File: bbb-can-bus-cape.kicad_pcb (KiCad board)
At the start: 2 copper layers, 54.6 x 86.4 mm, 93 parts, among them P1 BBB-DCAN0, P10 TERM, P11 TERM, P12 RS485, P15 MCP2512-CAN, P2 BBB-DCAN1, P3 TERM, P4 TERM, P5 TERM, P6 TERM, P7 MCP2515-CAN, P8 BeagleBone_Black_Header, P9 BeagleBone_Black_Header, Sw1 DTSM-31N, Sw2 DTSM-31N, Sw3 DTSM-31N, Sw4 DTSM-31N, U1 IFX1050GVIOXUMA1, U2 IFX1050GVIOXUMA1, U3 MCP2515_TSSOP20, U4 MCP2551, U5 TCN75A, U6 DS18B20U, U7 ISL3172EIUZ, U8 MCP2512_VDFN14, U9 MCP2551, X1 8MHZ, X2 8MHZ

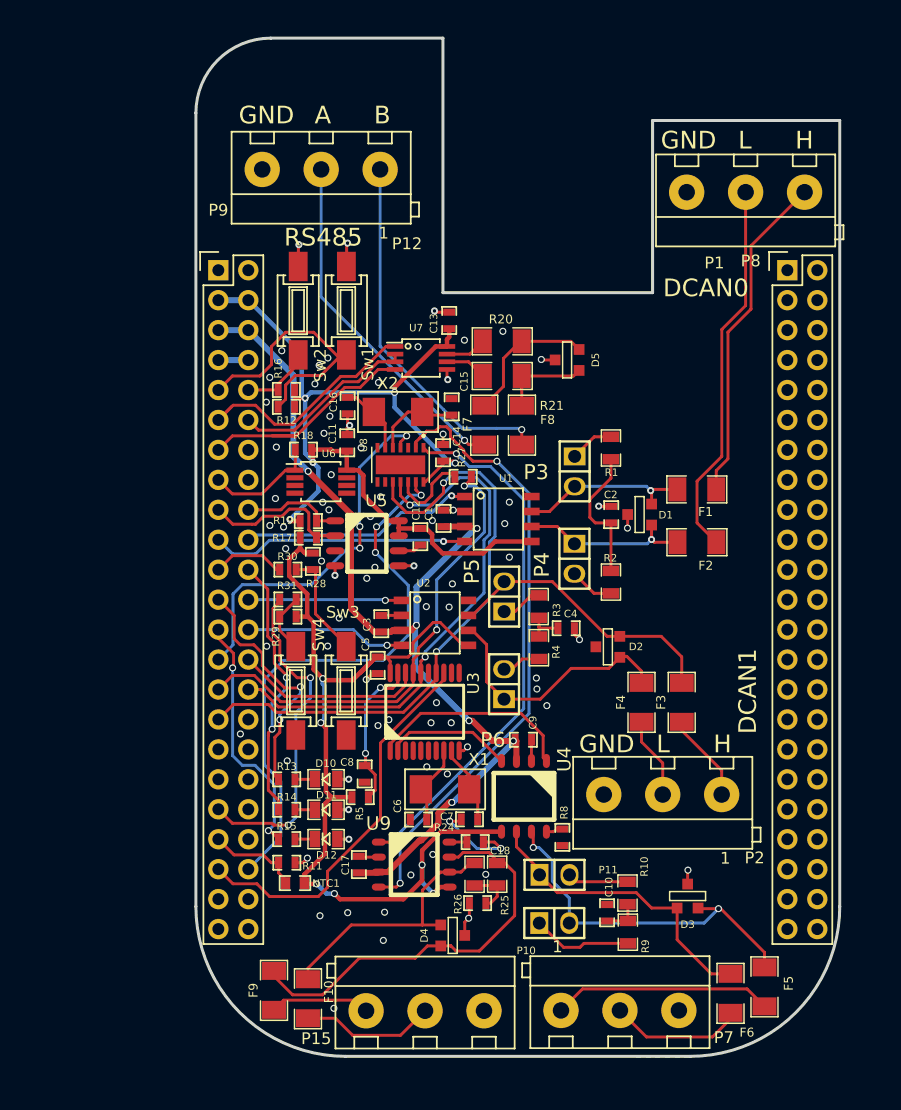
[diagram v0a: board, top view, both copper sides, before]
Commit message: created new layout for adjusted schematic
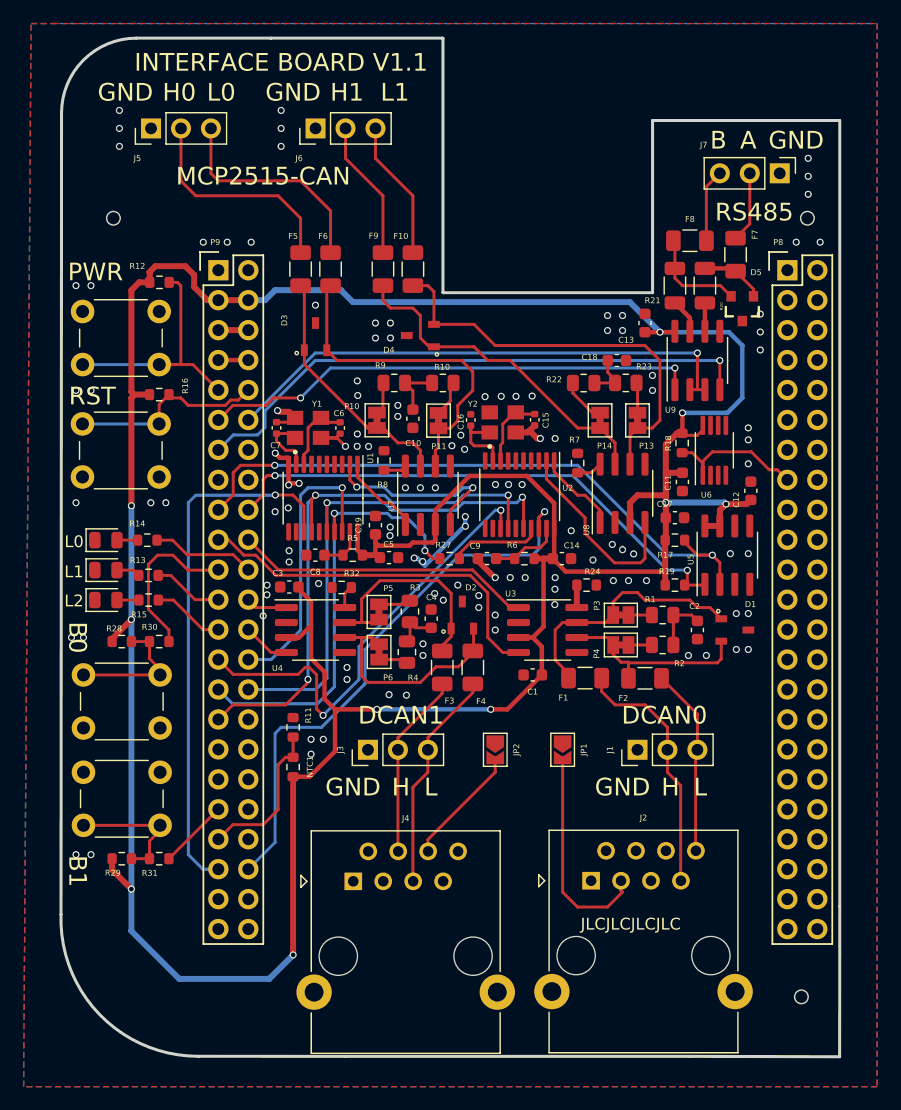
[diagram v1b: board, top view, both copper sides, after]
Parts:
- removed D10: LED_KP-2012HD, Diodes:LED_KP-2012HD_SM0805
- removed D11: LED_KP-2012SGD, Diodes:LED_KP-2012SGD_SM0805
- removed D12: LED_KP-2012YD, Diodes:LED_KP-2012YD_SM0805
- removed P1: BBB-DCAN0, Discrete_Connectors:DG301-5.0-03P-12-00A(H)
- removed P12: RS485, Discrete_Connectors:DG301-5.0-03P-12-00A(H)
- removed P15: MCP2512-CAN, Discrete_Connectors:DG301-5.0-03P-12-00A(H)
- removed P2: BBB-DCAN1, Discrete_Connectors:DG301-5.0-03P-12-00A(H)
- removed P7: MCP2515-CAN, Discrete_Connectors:DG301-5.0-03P-12-00A(H)
- removed R25, R26: 60.4R, Resistor_Smd_0805:60.4R_0805
- removed X1, X2: 8MHZ, Resonators:ABM3AIG-8.000MHZ-8-1R-T
- added C19: 100nF/50V, Capacitor_SMD:C_0603_1608Metric, F.Cu at (129.7, 84.0)
- added D6: LED, Diode_SMD:D_0805_2012Metric, F.Cu at (106.8, 87.8)
- added D7: LED, Diode_SMD:D_0805_2012Metric, F.Cu at (106.8, 85.3)
- added D8: LED, Diode_SMD:D_0805_2012Metric, F.Cu at (106.8, 90.4)
- added J1: Conn_DCAN0, Connector_PinHeader_2.54mm:PinHeader_1x03_P2.54mm_Vertical, F.Cu at (151.9, 103.1)
- added J2: RJ45 BBB-DCAN0, Connector_RJ:RJ45_Ninigi_GE, F.Cu at (148.0, 114.2)
- added J3: Conn_DCAN1, Connector_PinHeader_2.54mm:PinHeader_1x03_P2.54mm_Vertical, F.Cu at (129.1, 103.1)
- added J4: RJ45 BBB-DCAN1, Connector_RJ:RJ45_Ninigi_GE, F.Cu at (127.8, 114.2)
- added J5: Conn_MCP2515_CAN0, Connector_PinHeader_2.54mm:PinHeader_1x03_P2.54mm_Vertical, F.Cu at (110.7, 50.4)
- added J6: Conn_MCP2515_CAN1, Connector_PinHeader_2.54mm:PinHeader_1x03_P2.54mm_Vertical, F.Cu at (124.6, 50.4)
- added J7: Conn_RS485, Connector_PinHeader_2.54mm:PinHeader_1x03_P2.54mm_Vertical, F.Cu at (164.0, 54.2)
- added JP1: J2_Open, Jumper:SolderJumper-2_P1.3mm_Open_TrianglePad1.0x1.5mm, F.Cu at (145.6, 103.1)
- added JP2: J2_Open, Jumper:SolderJumper-2_P1.3mm_Open_TrianglePad1.0x1.5mm, F.Cu at (139.9, 103.1)
- added P13: TERM, Jumper:SolderJumper-2_P1.3mm_Bridged_Pad1.0x1.5mm, F.Cu at (148.7, 75.1)
- added P14: TERM, Jumper:SolderJumper-2_P1.3mm_Bridged_Pad1.0x1.5mm, F.Cu at (151.9, 75.1)
- added R22: 60R, Resistor_SMD:R_0805_2012Metric, F.Cu at (147.4, 72.0)
- added R23: 60R, Resistor_SMD:R_0805_2012Metric, F.Cu at (150.9, 71.9)
- added R32: 10k, Resistor_SMD:R_0603_1608Metric, F.Cu at (126.8, 89.3)
- added R6: 10k, Resistor_SMD:R_0603_1608Metric, F.Cu at (142.3, 86.8)
- added R7: 10k, Resistor_SMD:R_0603_1608Metric, F.Cu at (146.8, 78.7)
- added Y1: X322516MLB4SI, X322516MLB4SI:OSC_X322516MLB4SI, F.Cu at (124.0, 75.8)
- added Y2: X322516MLB4SI, X322516MLB4SI:OSC_X322516MLB4SI, F.Cu at (140.5, 75.3)
- C1, C10, C13, C14, C17, C18, C2, C3, C4, C5, C8, C9: footprint Capacitors_Smd_0603:100nF_0603 -> Capacitor_SMD:C_0603_1608Metric
- C11, C12: value 100n_50V -> 100nF/50V; footprint Capacitors_Smd_0603:100nF_0603 -> Capacitor_SMD:C_0603_1608Metric
- C15, C16, C6, C7: value 30pF/50V -> 10pF/50V; footprint Capacitors_Smd_0603:30pF_0603 -> Capacitor_SMD:C_0402_1005Metric
- D1, D2, D3, D4: value PESD2CAN -> PESD2CAN,215; footprint ESD_Protectors:PESD2CAN.215 -> PESD2CAN_215:SOT95P230X110-3N
- D5: value SM712.TCT -> PSM712; footprint ESD_Protectors:SM712.TCT -> PSM712:SOT23-3
- F1, F10, F2, F3, F4, F5, F6, F7, F8, F9: value SN005-60 -> Polyfuse_Small; footprint Smd_Ptc_Fuses:SN005-60 -> Fuse:Fuse_1206_3216Metric
- NTC1: footprint NTC_Thermistors:NTCS0603E3103FMT -> Resistor_SMD:R_0603_1608Metric
- P10, P11, P3, P4, P5, P6: footprint Goldpin:Goldpin_2_2_54mm -> Jumper:SolderJumper-2_P1.3mm_Bridged_Pad1.0x1.5mm
- R1, R10, R2, R3, R4, R9: value 60.4R -> 60R; footprint Resistor_Smd_0805:60.4R_0805 -> Resistor_SMD:R_0805_2012Metric
- R11, R12, R16, R17, R18, R19, R28, R29: footprint Resistor_Smd_0603:4k7_0603 -> Resistor_SMD:R_0603_1608Metric
- R13, R14, R15, R27, R30, R31: footprint Resistor_Smd_0603:100R_0603 -> Resistor_SMD:R_0603_1608Metric
- R20, R21: value CRCW120610R0FKEAHP -> 10R; footprint Resistor_Smd_1206:CRCW120610R0FKEAHP -> Resistor_SMD:R_1206_3216Metric
- R24, R8: value 100R -> 10k; footprint Resistor_Smd_0603:100R_0603 -> Resistor_SMD:R_0603_1608Metric
- R5: footprint Resistor_Smd_0603:10k_0603 -> Resistor_SMD:R_0603_1608Metric
- Sw1, Sw2, Sw3, Sw4: footprint Microswitches:DTSM-31N_SMD -> Button_Switch_THT:SW_PUSH_6mm
- U1, U2: value IFX1050GVIOXUMA1 -> MCP2515-xST; footprint Communication_Interfaces:IFX1050GVIOXUMA1 -> Package_SO:TSSOP-20_4.4x6.5mm_P0.65mm
- U3: value MCP2515_TSSOP20 -> SN65HVD230; footprint Communication_Interfaces:MCP2515-I-TSSOP20 -> Package_SO:SOIC-8_3.9x4.9mm_P1.27mm
- U4: value MCP2551 -> SN65HVD230; footprint Communication_Interfaces:MCP2551_SO8 -> Package_SO:SOIC-8_3.9x4.9mm_P1.27mm
- U5: footprint Temperature_Sensors:TCN75A_SOIC8 -> Package_SO:SOIC-8_3.9x4.9mm_P1.27mm
- U6: footprint Temperature_Sensors:DS18B20U_MSOP-8_3x3mm_P0.65mm -> Package_SO:MSOP-8_3x3mm_P0.65mm
- U7: value ISL3172EIUZ -> SN65HVD230; footprint Communication_Interfaces:ISL3172EIUZ -> Package_SO:SOIC-8_3.9x4.9mm_P1.27mm
- U8: value MCP2512_VDFN14 -> SN65HVD230; footprint Communication_Interfaces:MCP2512_VDFN14 -> Package_SO:SOIC-8_3.9x4.9mm_P1.27mm
- U9: value MCP2551 -> SP3485EN; footprint Communication_Interfaces:MCP2551_SO8 -> Package_SO:SOIC-8_3.9x4.9mm_P1.27mm
- moved F5 72.5 mm to (123.3, 62.3), turned to 90 degrees
- moved F6 70.2 mm to (125.9, 62.3), turned to 90 degrees
- moved F10 62.5 mm to (132.9, 62.3), turned to 90 degrees
- moved F9 61.9 mm to (130.3, 62.3), turned to 90 degrees
- moved D3 57.0 mm to (124.6, 68.0), turned to 90 degrees
- moved D4 51.0 mm to (133.5, 67.9), turned to 180 degrees
- moved R9 50.6 mm to (131.3, 71.9), turned to 0 degrees
- moved U9 49.0 mm to (157.0, 70.0), turned to 90 degrees
- moved C18 47.5 mm to (150.2, 70.0), turned to 0 degrees
- moved R10 46.0 mm to (135.4, 71.9), turned to 0 degrees
- moved P10 45.2 mm to (129.8, 75.1), turned to -90 degrees
- moved C10 45.0 mm to (132.9, 75.0), turned to -90 degrees
- moved C17 39.8 mm to (155.1, 83.4), turned to 0 degrees
- moved P11 39.8 mm to (135.0, 75.1), turned to 90 degrees
- moved C7 37.0 mm to (121.3, 75.8), turned to 90 degrees
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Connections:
- C1 pad 1: 5V -> 3V3
- C15 pad 1: Net-(C15-Pad1) -> Net-(U2-OSC2)
- C16 pad 1: Net-(C16-Pad1) -> Net-(U2-OSC1)
- C17 pad 1: 5V -> 3V3
- C3 pad 1: 5V -> 3V3
- C6 pad 1: Net-(C6-Pad1) -> Net-(U1-OSC2)
- C7 pad 1: Net-(C7-Pad1) -> Net-(U1-OSC1)
- C8 pad 1: Net-(C8-Pad1) -> Net-(U1-~{RESET})
- C9 pad 1: 5V -> Net-(U2-~{RESET})
- D1 pad 1: Net-(D1-Pad1) -> Net-(U3-CANH)
- D1 pad 2: Net-(D1-Pad2) -> Net-(U3-CANL)
- D2 pad 1: Net-(D2-Pad1) -> Net-(U4-CANH)
- D2 pad 2: Net-(D2-Pad2) -> Net-(U4-CANL)
- D3 pad 1: Net-(D3-Pad1) -> Net-(U7-CANH)
- D3 pad 2: Net-(D3-Pad2) -> Net-(U7-CANL)
- D4 pad 1: Net-(D4-Pad1) -> Net-(U8-CANH)
- D4 pad 2: Net-(D4-Pad2) -> Net-(U8-CANL)
- F1 pad 1: Net-(D1-Pad2) -> Net-(U3-CANH)
- F10 pad 1: Net-(D4-Pad1) -> Net-(U8-CANL)
- F2 pad 1: Net-(D1-Pad1) -> Net-(U3-CANL)
- F3 pad 1: Net-(D2-Pad2) -> Net-(U4-CANH)
- F4 pad 1: Net-(D2-Pad1) -> Net-(U4-CANL)
- F5 pad 1: Net-(D3-Pad2) -> Net-(U7-CANH)
- F6 pad 1: Net-(D3-Pad1) -> Net-(U7-CANL)
- F7 pad 1: Net-(D5-Pad2) -> Net-(D5-Pad1)
- F7 pad 2: /RS485/RS485_B -> /RS485/RS485_A
- F8 pad 1: Net-(D5-Pad1) -> Net-(D5-Pad2)
- F8 pad 2: /RS485/RS485_A -> /RS485/RS485_B
- F9 pad 1: Net-(D4-Pad2) -> Net-(U8-CANH)
- P10 pad 2: Net-(D3-Pad2) -> Net-(U7-CANH)
- P11 pad 1: Net-(D3-Pad1) -> Net-(U7-CANL)
- P3 pad 2: Net-(D1-Pad2) -> Net-(U3-CANH)
- P4 pad 1: Net-(D1-Pad1) -> Net-(U3-CANL)
- P5 pad 2: Net-(D2-Pad2) -> Net-(U4-CANH)
- P6 pad 1: Net-(D2-Pad1) -> Net-(U4-CANL)
- P8 pad 10: (no net) -> unconnected-(P8-Pin_10-Pad10)
- P8 pad 11: (no net) -> unconnected-(P8-Pin_11-Pad11)
- P8 pad 12: (no net) -> unconnected-(P8-Pin_12-Pad12)
- P8 pad 13: (no net) -> unconnected-(P8-Pin_13-Pad13)
- P8 pad 14: (no net) -> unconnected-(P8-Pin_14-Pad14)
- P8 pad 15: (no net) -> Net-(P8-Pin_15)
- P8 pad 16: (no net) -> unconnected-(P8-Pin_16-Pad16)
- P8 pad 17: (no net) -> unconnected-(P8-Pin_17-Pad17)
- P8 pad 18: (no net) -> unconnected-(P8-Pin_18-Pad18)
- P8 pad 19: (no net) -> unconnected-(P8-Pin_19-Pad19)
- P8 pad 20: (no net) -> unconnected-(P8-Pin_20-Pad20)
- P8 pad 21: (no net) -> unconnected-(P8-Pin_21-Pad21)
- P8 pad 22: (no net) -> unconnected-(P8-Pin_22-Pad22)
- P8 pad 23: (no net) -> unconnected-(P8-Pin_23-Pad23)
- P8 pad 24: (no net) -> unconnected-(P8-Pin_24-Pad24)
- P8 pad 25: (no net) -> unconnected-(P8-Pin_25-Pad25)
- P8 pad 26: (no net) -> unconnected-(P8-Pin_26-Pad26)
- P8 pad 27: (no net) -> unconnected-(P8-Pin_27-Pad27)
- P8 pad 28: (no net) -> unconnected-(P8-Pin_28-Pad28)
- P8 pad 29: (no net) -> unconnected-(P8-Pin_29-Pad29)
- P8 pad 3: (no net) -> unconnected-(P8-Pin_3-Pad3)
- P8 pad 30: (no net) -> unconnected-(P8-Pin_30-Pad30)
- P8 pad 31: (no net) -> unconnected-(P8-Pin_31-Pad31)
- P8 pad 32: (no net) -> unconnected-(P8-Pin_32-Pad32)
- P8 pad 33: (no net) -> unconnected-(P8-Pin_33-Pad33)
- P8 pad 34: (no net) -> unconnected-(P8-Pin_34-Pad34)
- P8 pad 35: (no net) -> unconnected-(P8-Pin_35-Pad35)
- P8 pad 36: (no net) -> unconnected-(P8-Pin_36-Pad36)
- P8 pad 37: (no net) -> unconnected-(P8-Pin_37-Pad37)
- P8 pad 38: (no net) -> unconnected-(P8-Pin_38-Pad38)
- P8 pad 39: (no net) -> unconnected-(P8-Pin_39-Pad39)
- P8 pad 4: (no net) -> unconnected-(P8-Pin_4-Pad4)
- P8 pad 40: (no net) -> unconnected-(P8-Pin_40-Pad40)
- P8 pad 41: (no net) -> unconnected-(P8-Pin_41-Pad41)
- P8 pad 42: (no net) -> unconnected-(P8-Pin_42-Pad42)
- P8 pad 43: (no net) -> unconnected-(P8-Pin_43-Pad43)
- P8 pad 44: (no net) -> unconnected-(P8-Pin_44-Pad44)
- P8 pad 45: (no net) -> unconnected-(P8-Pin_45-Pad45)
- P8 pad 46: (no net) -> unconnected-(P8-Pin_46-Pad46)
- P8 pad 5: (no net) -> unconnected-(P8-Pin_5-Pad5)
- P8 pad 6: (no net) -> unconnected-(P8-Pin_6-Pad6)
- P8 pad 7: (no net) -> unconnected-(P8-Pin_7-Pad7)
- P8 pad 8: (no net) -> unconnected-(P8-Pin_8-Pad8)
- P8 pad 9: (no net) -> unconnected-(P8-Pin_9-Pad9)
- P9 pad 14: (no net) -> unconnected-(P9-Pin_14-Pad14)
- P9 pad 15: Net-(P9-Pad15) -> unconnected-(P9-Pin_15-Pad15)
- P9 pad 16: (no net) -> unconnected-(P9-Pin_16-Pad16)
- P9 pad 27: /Standalone Can BUS/CAN_~INT1~ -> /Standalone Can BUS/CAN_~{INT1}
- P9 pad 32: (no net) -> VCC-RTC
- P9 pad 33: (no net) -> unconnected-(P9-Pin_33-Pad33)
- P9 pad 34: (no net) -> GNDA
- P9 pad 35: (no net) -> unconnected-(P9-Pin_35-Pad35)
- P9 pad 36: (no net) -> unconnected-(P9-Pin_36-Pad36)
- P9 pad 38: (no net) -> unconnected-(P9-Pin_38-Pad38)
- P9 pad 40: (no net) -> unconnected-(P9-Pin_40-Pad40)
- R18 pad 2: Net-(P9-Pad15) -> Net-(P8-Pin_15)
- R20 pad 1: Net-(D5-Pad2) -> Net-(U9-A)
- R20 pad 2: Net-(R20-Pad2) -> Net-(D5-Pad1)
- R21 pad 1: Net-(D5-Pad1) -> Net-(U9-B)
- R21 pad 2: Net-(R21-Pad2) -> Net-(D5-Pad2)
- R24 pad 1: Net-(R24-Pad1) -> Net-(U3-Rs)
- R27 pad 2: Net-(R27-Pad2) -> Net-(U2-SO)
- R5 pad 1: Net-(C8-Pad1) -> Net-(U1-~{RESET})
- R8 pad 1: Net-(R8-Pad1) -> Net-(U7-Rs)
- U1 pad 1: /DCAN0_TX -> Net-(U1-TXCAN)
- U1 pad 2: GND -> Net-(U1-RXCAN)
- U1 pad 3: 5V -> unconnected-(U1-CLKOUT/SOF-Pad3)
- U1 pad 4: /DCAN0_RX -> unconnected-(U1-~{TX0RTS}-Pad4)
- U1 pad 5: 3V3 -> unconnected-(U1-~{TX1RTS}-Pad5)
- U1 pad 6: Net-(D1-Pad1) -> unconnected-(U1-NC-Pad6)
- U1 pad 7: Net-(D1-Pad2) -> unconnected-(U1-~{TX2RTS}-Pad7)
- U1 pad 8: GND -> Net-(U1-OSC2)
- U2 pad 1: /DCAN1_RX -> Net-(U2-TXCAN)
- U2 pad 2: GND -> Net-(U2-RXCAN)
- U2 pad 3: 5V -> unconnected-(U2-CLKOUT/SOF-Pad3)
- U2 pad 4: /DCAN1_TX -> unconnected-(U2-~{TX0RTS}-Pad4)
- U2 pad 5: 3V3 -> unconnected-(U2-~{TX1RTS}-Pad5)
- U2 pad 6: Net-(D2-Pad1) -> unconnected-(U2-NC-Pad6)
- U2 pad 7: Net-(D2-Pad2) -> unconnected-(U2-~{TX2RTS}-Pad7)
- U2 pad 8: GND -> Net-(U2-OSC2)
- U3 pad 1: Net-(U3-Pad1) -> /DCAN0_TX
- U3 pad 2: Net-(U3-Pad2) -> GND
- U3 pad 3: (no net) -> 3V3
- U3 pad 4: (no net) -> /DCAN0_RX
- U3 pad 5: (no net) -> unconnected-(U3-Vref-Pad5)
- U3 pad 6: (no net) -> Net-(U3-CANL)
- U3 pad 7: (no net) -> Net-(U3-CANH)
- U3 pad 8: Net-(C6-Pad1) -> Net-(U3-Rs)
- U4 pad 1: Net-(U3-Pad1) -> /DCAN1_RX
- U4 pad 3: 5V -> 3V3
- U4 pad 4: Net-(U3-Pad2) -> /DCAN1_TX
- U4 pad 5: 3V3 -> unconnected-(U4-Vref-Pad5)
- U4 pad 6: Net-(D3-Pad1) -> Net-(U4-CANL)
- U4 pad 7: Net-(D3-Pad2) -> Net-(U4-CANH)
- U4 pad 8: Net-(R8-Pad1) -> Net-(U4-Rs)
- U5 pad 3: (no net) -> unconnected-(U5-ALERT-Pad3)
- U6 pad 1: Net-(P9-Pad15) -> Net-(P8-Pin_15)
- U6 pad 2: (no net) -> unconnected-(U6-NC-Pad2)
- U6 pad 3: (no net) -> unconnected-(U6-NC-Pad3)
- U6 pad 5: (no net) -> unconnected-(U6-N-Pad5)
- U6 pad 6: (no net) -> unconnected-(U6-NC-Pad6)
- U6 pad 7: (no net) -> unconnected-(U6-NC-Pad7)
- U7 pad 1: /UART4_RX -> Net-(U1-TXCAN)
- U7 pad 2: /GPIO1_28 -> GND
- U7 pad 3: /GPIO1_28 -> 3V3
- U7 pad 4: /UART4_TX -> Net-(U1-RXCAN)
- U7 pad 5: GND -> unconnected-(U7-Vref-Pad5)
- U7 pad 6: Net-(R21-Pad2) -> Net-(U7-CANL)
- U7 pad 7: Net-(R20-Pad2) -> Net-(U7-CANH)
- U7 pad 8: 3V3 -> Net-(U7-Rs)
- U8 pad 1: Net-(U8-Pad1) -> Net-(U2-TXCAN)
- U8 pad 2: Net-(U8-Pad2) -> GND
- U8 pad 3: (no net) -> 3V3
- U8 pad 4: /Standalone Can BUS/CAN_~INT1~ -> Net-(U2-RXCAN)
- U8 pad 5: Net-(C15-Pad1) -> unconnected-(U8-Vref-Pad5)
- U8 pad 6: Net-(C16-Pad1) -> Net-(U8-CANL)
- U8 pad 7: GND -> Net-(U8-CANH)
- U8 pad 8: (no net) -> Net-(U8-Rs)
- U9 pad 1: Net-(U8-Pad1) -> /UART4_RX
- U9 pad 2: GND -> /GPIO1_28
- U9 pad 3: 5V -> /GPIO1_28
- U9 pad 4: Net-(U8-Pad2) -> /UART4_TX
- U9 pad 5: 3V3 -> GND
- U9 pad 6: Net-(D4-Pad1) -> Net-(U9-A)
- U9 pad 7: Net-(D4-Pad2) -> Net-(U9-B)
- U9 pad 8: Net-(R24-Pad1) -> 3V3
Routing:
- net 3V3: track 165.9 -> 292.6 mm, vias 11 -> 10
- net 5V: track 86.4 -> 2.54 mm, vias 6 -> 0
- net Net-(U8-Pad2): track 53.7 -> 0.00 mm, vias 2 -> 0
- net Net-(U8-Pad1): track 45.0 -> 0.00 mm, vias 2 -> 0
- net /I2C1_SCL: track 12.8 -> 53.5 mm, vias 0 -> 2
- net /Standalone Can BUS/CAN_~{INT1}: track 0.00 -> 38.5 mm, vias 0 -> 2
- net /I2C1_SDA: track 8.69 -> 45.6 mm, vias 0 -> 2
- net Net-(U8-CANL): track 0.00 -> 35.8 mm
- net Net-(D4-Pad2): track 34.8 -> 0.00 mm
- net /Standalone Can BUS/CAN_~INT1~: track 31.6 -> 0.00 mm, vias 3 -> 0
- net Net-(D3-Pad2): track 31.0 -> 0.00 mm, vias 2 -> 0
- net /UART4_TX: track 19.9 -> 49.0 mm, vias 0 -> 1
- net /GPIO1_28: track 15.9 -> 44.8 mm, vias 0 -> 1
- net Net-(U8-CANH): track 0.00 -> 28.9 mm
- net Net-(U7-CANL): track 0.00 -> 28.7 mm
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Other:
- board size 54.6 x 86.4 mm -> 66 x 86.4 mm
- board text added: "B0"
- board text added: "B1"
- board text added: "H0"
- board text added: "H1"
- board text added: "INTERFACE BOARD V1.1"
- board text added: "JLCJLCJLCJLC"
- board text added: "L0"
- board text added: "L1"
- board text added: "L2"
- board text added: "PWR"
- board text added: "RST"
- board text removed: "INTERFACE BOARD V1.0"
- board text removed: "MCP2512-CAN"
